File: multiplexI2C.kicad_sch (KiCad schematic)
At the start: 24 parts, among them J17 Conn_01x04_Pin, J18 PinSocket_1x20_P2.54mm_Vertic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, J19 PinSocket_1x20_P2.54mm_Vertic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, J20 Screw_Terminal_01x02, J9 header_0.25sqmm_1x04_P4.2mm_D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, SW1 SW_DIP_x03, U1 TCA9548A

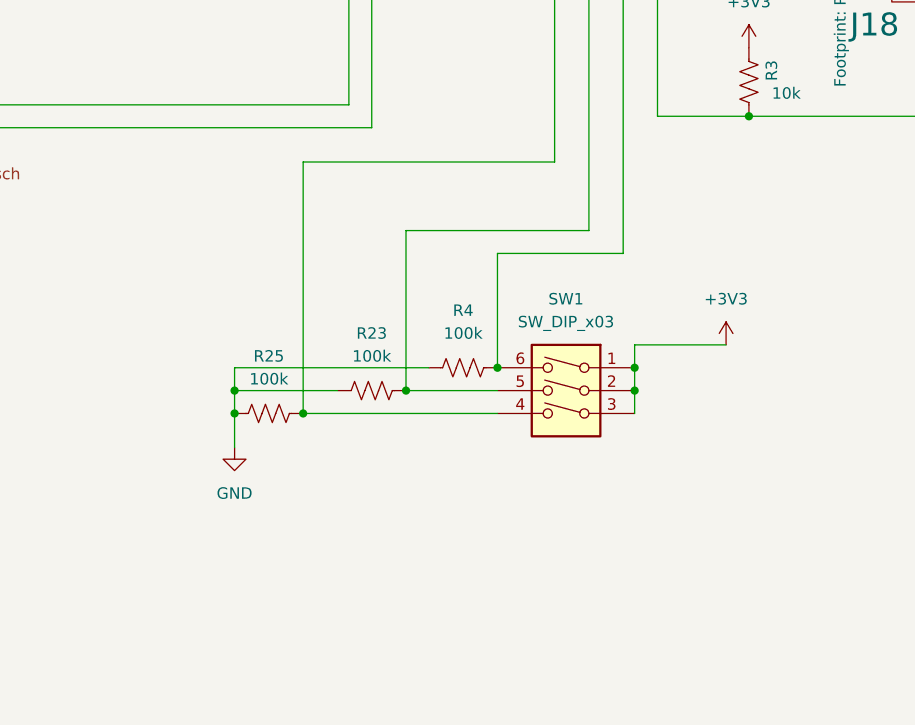
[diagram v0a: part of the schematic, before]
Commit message: replaced address switch with R0 changeable by solder.
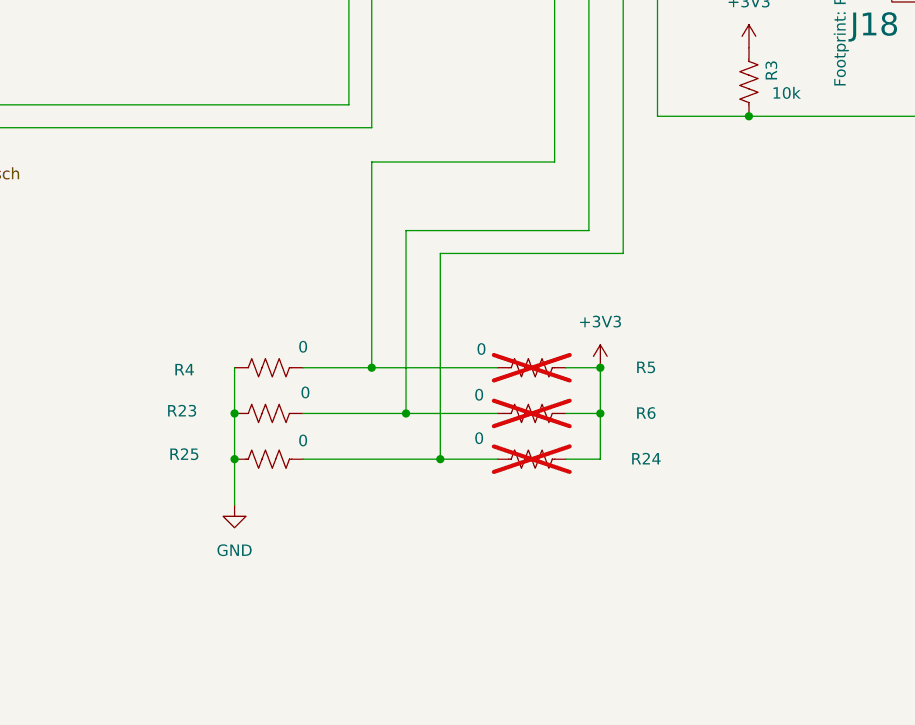
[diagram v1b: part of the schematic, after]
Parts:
- removed SW1: SW_DIP_x03, ProjectLib:SW_DIP_SPSTx03_Slide_KingTek_DSHP03TS_W7.62mm_P1.27mm, symbol ProjectLib:SW_DIP_x03
- added R24, R5, R6: 0, ProjectLib:R_0603_1608Metric, symbol ProjectLib:R_US
- R23, R25, R4: value 100k -> 0
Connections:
- net +3V3: now also R24.1, R5.1, R6.1
- net at R23.1, U1.2 (A1): now also R6.2
- net at R25.1: now also U1.21 (A2), R24.2; no longer U1.1 (A0)
- net at R4.1: now also U1.1 (A0), R5.2; no longer U1.21 (A2)
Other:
- moved on the sheet: R23, R25, R4

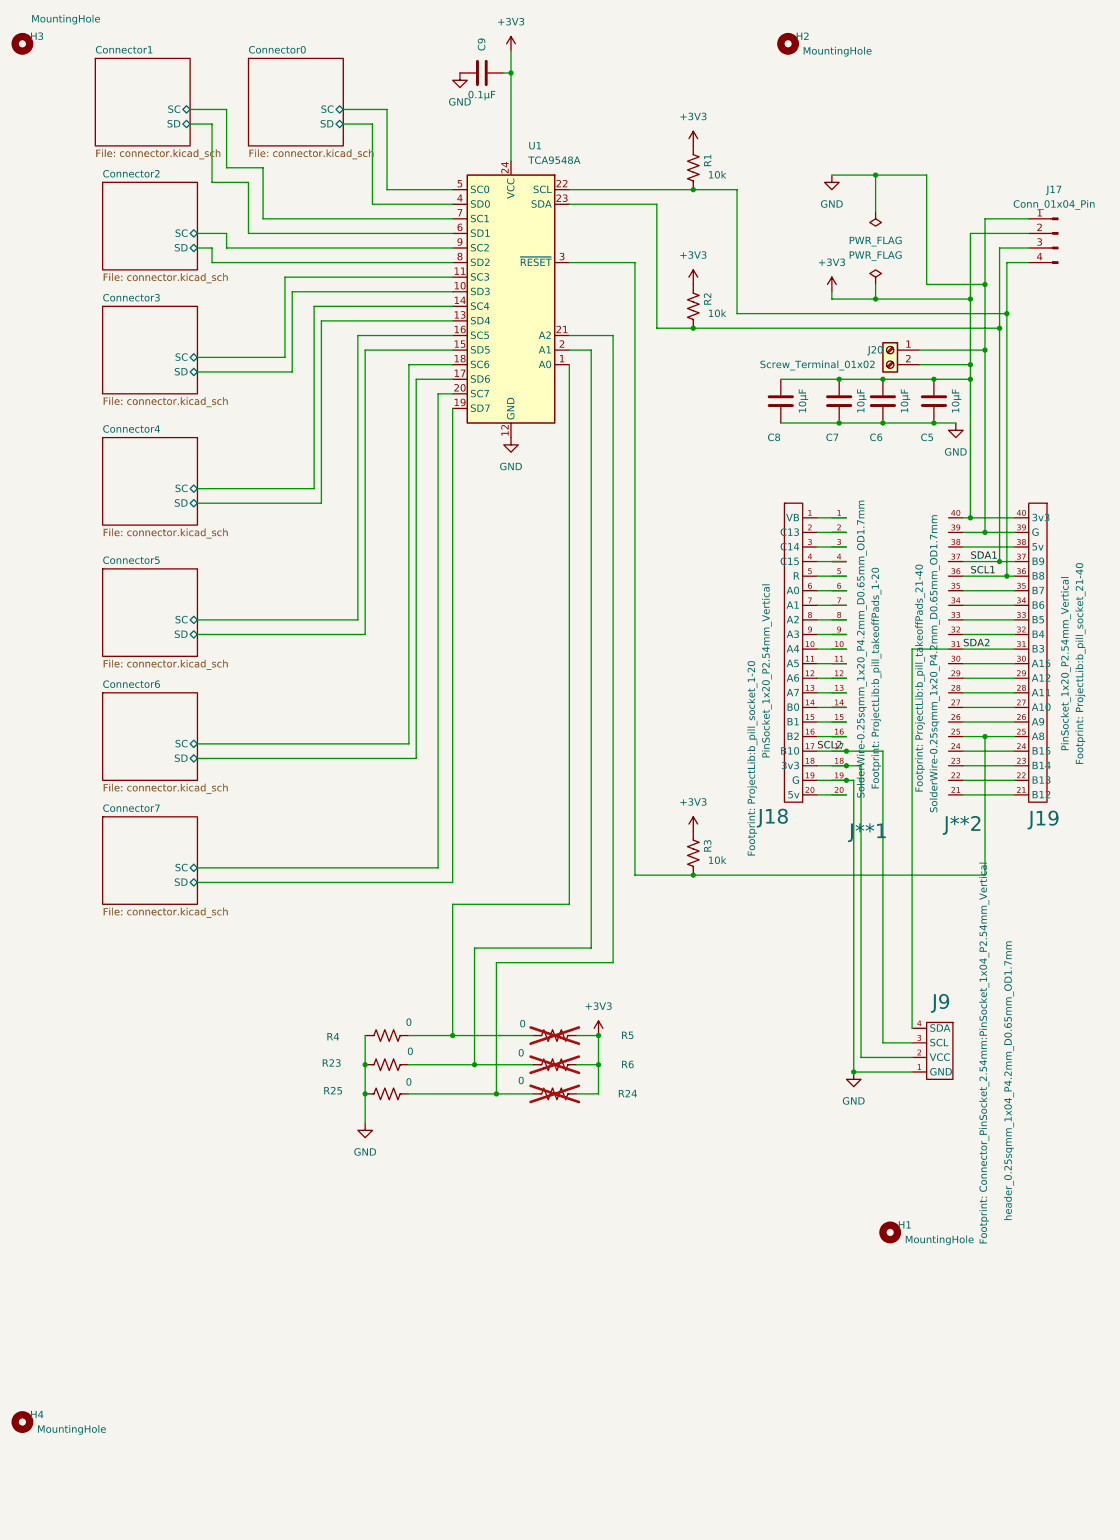
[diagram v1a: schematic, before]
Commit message: added RFM95W pad for sx127x, unpopulated.
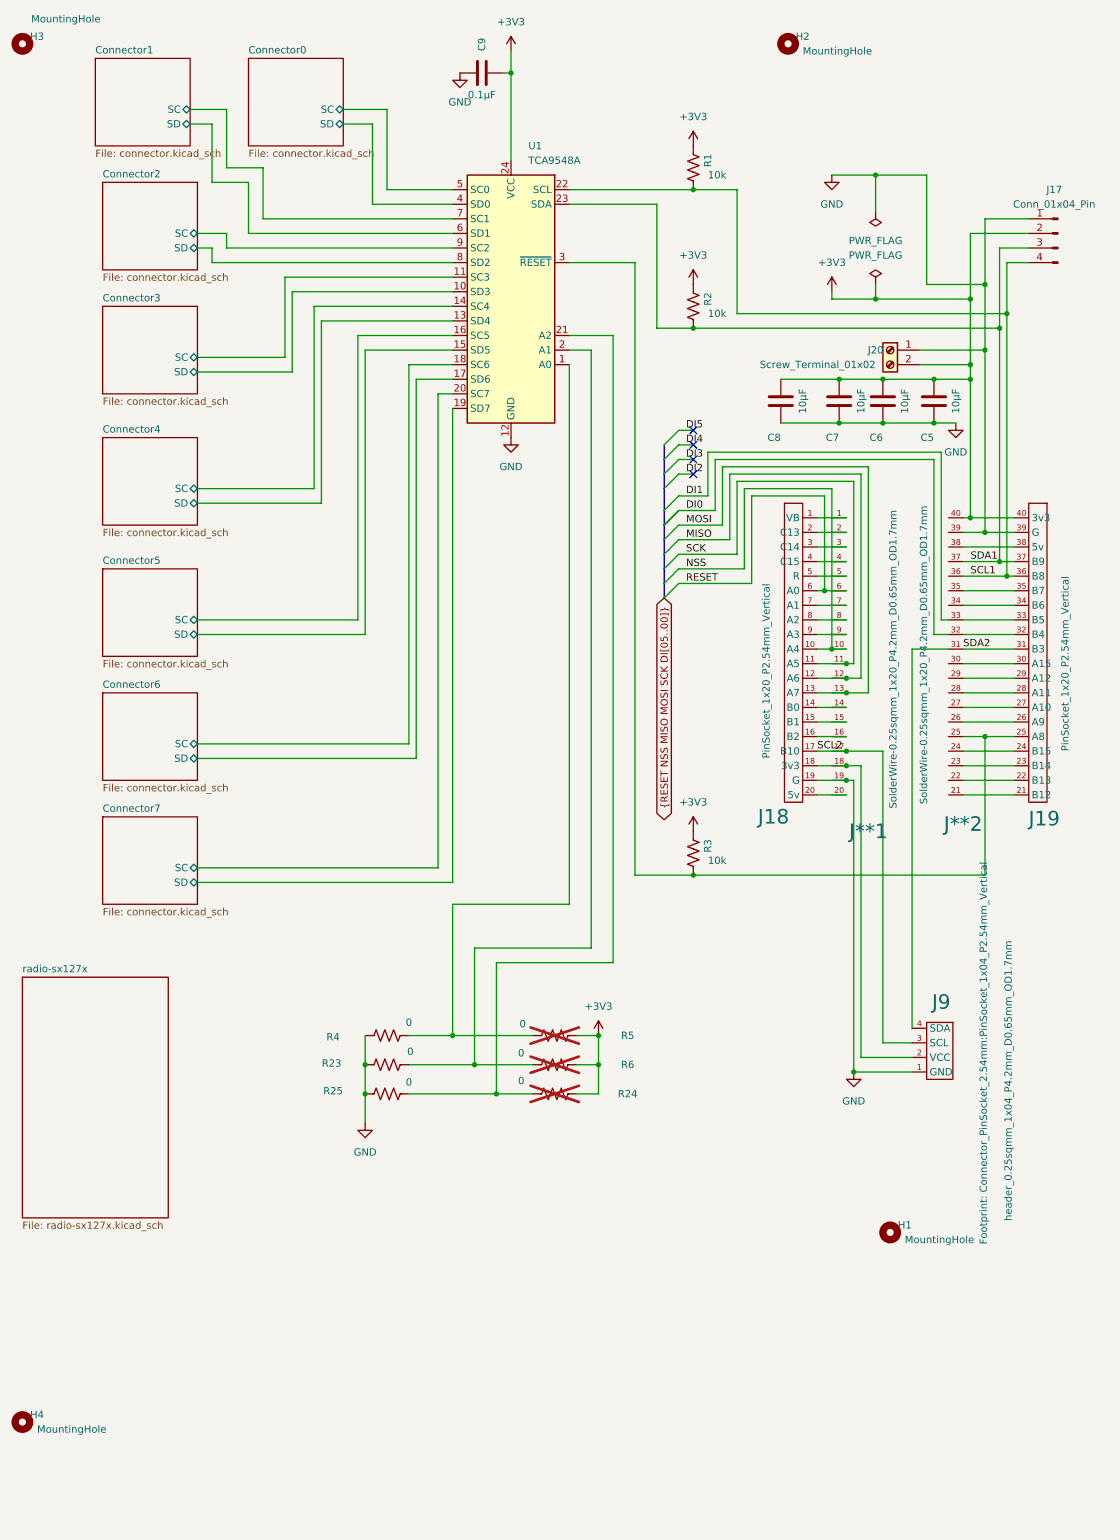
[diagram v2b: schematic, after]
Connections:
- net NSS: now reaches J**1.10, J18.10 (A4)
- net SCK: now reaches J**1.11, J18.11 (A5)
- net MISO: now reaches J**1.12, J18.12 (A6)
- net MOSI: now reaches J**1.13, J18.13 (A7)
- net RESET: now reaches J**1.6, J18.6 (A0)
- no-connect marks 0 -> 4
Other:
- added sheet radio-sx127x (radio-sx127x.kicad_sch)

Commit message: e220 schematic needs work, and proper DIO connections. Switching back to radio-sx127.
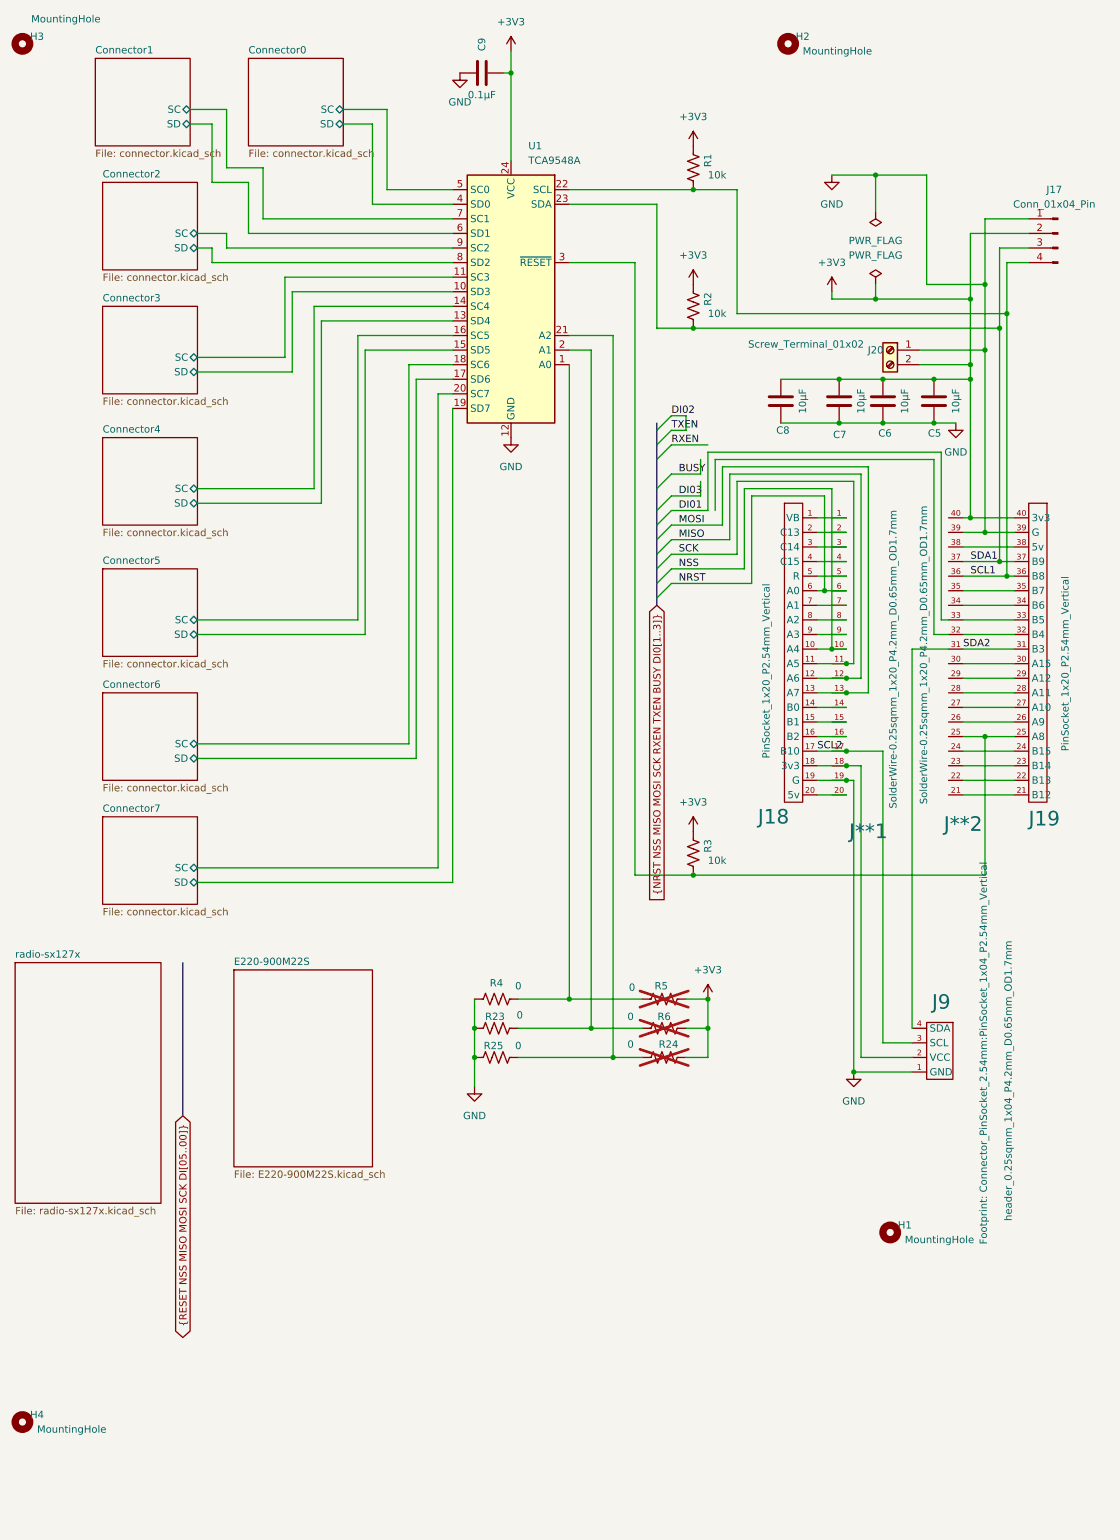
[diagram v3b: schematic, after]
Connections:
- net RESET renamed NRST
- no-connect marks 4 -> 0
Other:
- added sheet E220-900M22S (E220-900M22S.kicad_sch)
- moved on the sheet: R23, R24, R25, R4, R5, R6

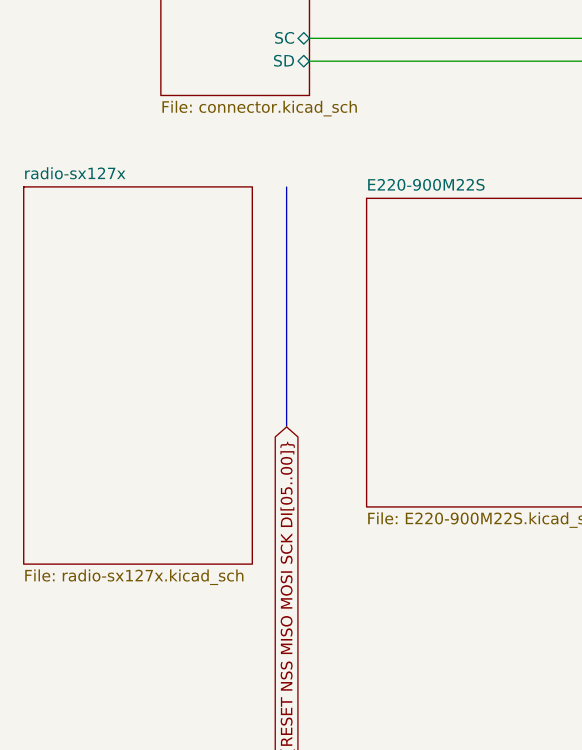
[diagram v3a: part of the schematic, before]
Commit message: renamed radio-sx127x.kicad_sch to RFM95W.kicad_sch
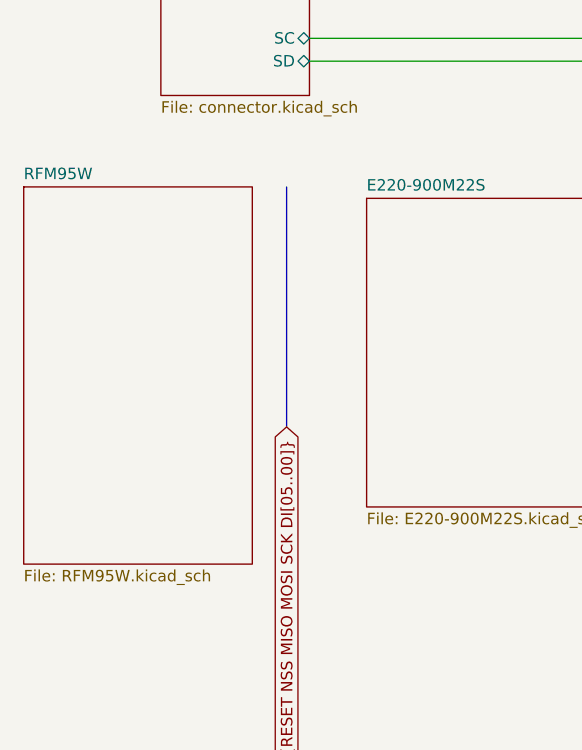
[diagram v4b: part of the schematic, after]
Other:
- sheet radio-sx127x renamed RFM95W
- sheet RFM95W: file radio-sx127x.kicad_sch -> RFM95W.kicad_sch
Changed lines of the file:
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@@
 	(label "MOSI"
 		(at 133.35 104.14 0)
+		(fields_autoplaced yes)
 		(effects
 			(font
@@
 	(label "NSS"
 		(at 133.35 111.76 0)
+		(fields_autoplaced yes)
 		(effects
 			(font
@@
 	(label "TXEN"
 		(at 132.08 87.63 0)
+		(fields_autoplaced yes)
 		(effects
 			(font
@@
 	(label "DI02"
 		(at 132.08 85.09 0)
+		(fields_autoplaced yes)
 		(effects
 			(font
@@
 	(label "NRST"
 		(at 133.35 114.3 0)
+		(fields_autoplaced yes)
 		(effects
 			(font
@@
 	(label "MISO"
 		(at 133.35 106.68 0)
+		(fields_autoplaced yes)
 		(effects
 			(font
@@
 	(label "SCK"
 		(at 133.35 109.22 0)
+		(fields_autoplaced yes)
 		(effects
 			(font
@@
 	(label "RXEN"
 		(at 132.08 90.17 0)
+		(fields_autoplaced yes)
 		(effects
 			(font
@@
 	(label "DI03"
 		(at 133.35 99.06 0)
+		(fields_autoplaced yes)
 		(effects
 			(font
@@
 	(label "DI01"
 		(at 133.35 101.6 0)
+		(fields_autoplaced yes)
 		(effects
 			(font
@@
 	(label "BUSY"
 		(at 133.35 95.25 0)
+		(fields_autoplaced yes)
 		(effects
 			(font
@@
 			(color 0 0 0 0.0000)
 		)
-		(property "Sheetname" "radio-sx127x"
+		(property "Sheetname" "RFM95W"
 			(at 17.78 179.6284 0)
 			(effects
@@
 			)
 		)
-		(property "Sheetfile" "radio-sx127x.kicad_sch"
+		(property "Sheetfile" "RFM95W.kicad_sch"
 			(at 17.78 222.8346 0)
 			(effects

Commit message: some cleanup. About to split two lra module branches.
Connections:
- net SDA2: now also J9.4 (SDA)
- net DIO0: now reaches J**2.32, J19.32 (B4)
- net DIO1: now reaches J**2.33, J19.33 (B5)
- net NRST renamed RESET
